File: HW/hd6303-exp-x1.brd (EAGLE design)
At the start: 100 x 80 mm, 40 parts, among them IC1 74HC245N, IC2 74HC245N, IC3 74HC245N, IC4 LM386N-1

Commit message: pullup for page_a13-page_a17, fixed decoder rom
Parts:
- C1, C10, C3, C4, C5, C6, C7, C8, C9: value (none) -> 100n
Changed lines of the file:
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@@
 <attribute name="NAME" x="12.065" y="18.415" size="1.27" layer="26" rot="MR270"/>
 </element>
-<element name="C4" library="rcl" package="C0603" value="" x="66.04" y="5.08" smashed="yes" rot="MR180">
+<element name="C4" library="rcl" package="C0603" value="100n" x="66.04" y="5.08" smashed="yes" rot="MR180">
 <attribute name="NAME" x="65.405" y="4.445" size="1.27" layer="26" rot="MR180"/>
 <attribute name="VALUE" x="65.405" y="6.985" size="1.27" layer="28" rot="MR180"/>
 </element>
-<element name="C5" library="rcl" package="C0603" value="" x="62.23" y="43.18" smashed="yes" rot="MR270">
+<element name="C5" library="rcl" package="C0603" value="100n" x="62.23" y="43.18" smashed="yes" rot="MR270">
 <attribute name="NAME" x="61.595" y="43.815" size="1.27" layer="26" rot="MR270"/>
 <attribute name="VALUE" x="64.135" y="43.815" size="1.27" layer="28" rot="MR270"/>
 </element>
-<element name="C6" library="rcl" package="C0603" value="" x="15.24" y="16.51" smashed="yes" rot="MR90">
+<element name="C6" library="rcl" package="C0603" value="100n" x="15.24" y="16.51" smashed="yes" rot="MR90">
 <attribute name="NAME" x="15.875" y="15.875" size="1.27" layer="26" rot="MR90"/>
 <attribute name="VALUE" x="13.335" y="15.875" size="1.27" layer="28" rot="MR90"/>
 </element>
-<element name="C7" library="rcl" package="C0603" value="" x="24.13" y="17.78" smashed="yes" rot="MR90">
+<element name="C7" library="rcl" package="C0603" value="100n" x="24.13" y="17.78" smashed="yes" rot="MR90">
 <attribute name="NAME" x="24.765" y="17.145" size="1.27" layer="26" rot="MR90"/>
 <attribute name="VALUE" x="22.225" y="17.145" size="1.27" layer="28" rot="MR90"/>
 </element>
-<element name="C8" library="rcl" package="C0603" value="" x="12.7" y="54.61" smashed="yes" rot="MR90">
+<element name="C8" library="rcl" package="C0603" value="100n" x="12.7" y="54.61" smashed="yes" rot="MR90">
 <attribute name="NAME" x="13.335" y="53.975" size="1.27" layer="26" rot="MR90"/>
 <attribute name="VALUE" x="10.795" y="53.975" size="1.27" layer="28" rot="MR90"/>
 </element>
-<element name="C9" library="rcl" package="C0603" value="" x="24.13" y="54.61" smashed="yes" rot="MR90">
+<element name="C9" library="rcl" package="C0603" value="100n" x="24.13" y="54.61" smashed="yes" rot="MR90">
 <attribute name="NAME" x="24.765" y="53.975" size="1.27" layer="26" rot="MR90"/>
 <attribute name="VALUE" x="22.225" y="53.975" size="1.27" layer="28" rot="MR90"/>
 </element>
-<element name="C10" library="rcl" package="C0603" value="" x="81.28" y="46.99" smashed="yes" rot="MR180">
+<element name="C10" library="rcl" package="C0603" value="100n" x="81.28" y="46.99" smashed="yes" rot="MR180">
 <attribute name="NAME" x="80.645" y="46.355" size="1.27" layer="26" rot="MR180"/>
 <attribute name="VALUE" x="80.645" y="48.895" size="1.27" layer="28" rot="MR180"/>
@@
 <attribute name="NAME" x="53.34" y="6.35" size="1.27" layer="26" rot="MR0"/>
 </element>
-<element name="C1" library="rcl" package="C0603" value="" x="81.28" y="5.08" smashed="yes" rot="MR180">
+<element name="C1" library="rcl" package="C0603" value="100n" x="81.28" y="5.08" smashed="yes" rot="MR180">
 <attribute name="NAME" x="80.645" y="4.445" size="1.27" layer="26" rot="MR180"/>
 <attribute name="VALUE" x="80.645" y="6.985" size="1.27" layer="28" rot="MR180"/>
@@
 <attribute name="NAME" x="38.1" y="52.07" size="1.27" layer="26" rot="MR90"/>
 </element>
-<element name="C3" library="rcl" package="C0603" value="" x="53.34" y="62.23" smashed="yes" rot="MR270">
+<element name="C3" library="rcl" package="C0603" value="100n" x="53.34" y="62.23" smashed="yes" rot="MR270">
 <attribute name="NAME" x="52.705" y="62.865" size="1.27" layer="26" rot="MR270"/>
 <attribute name="VALUE" x="55.245" y="62.865" size="1.27" layer="28" rot="MR270"/>

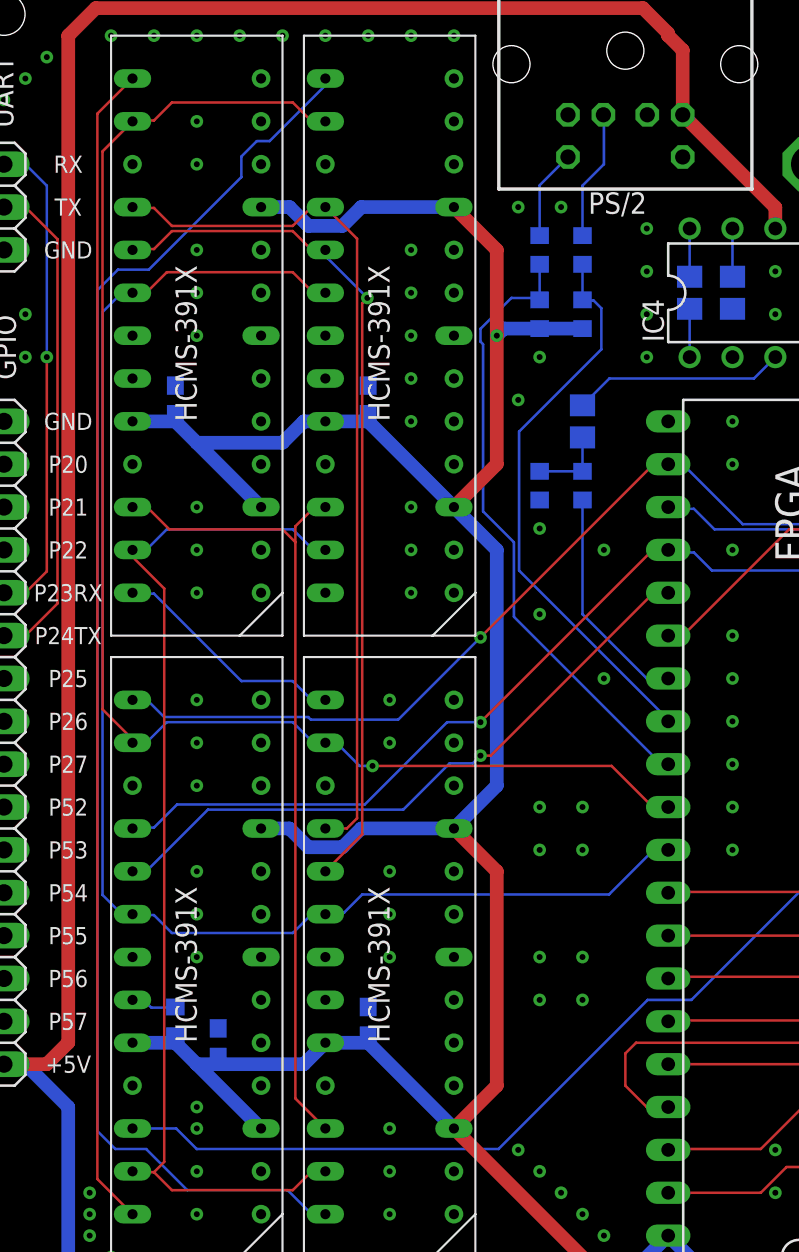
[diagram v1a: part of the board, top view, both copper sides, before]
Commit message: fixed missed nets
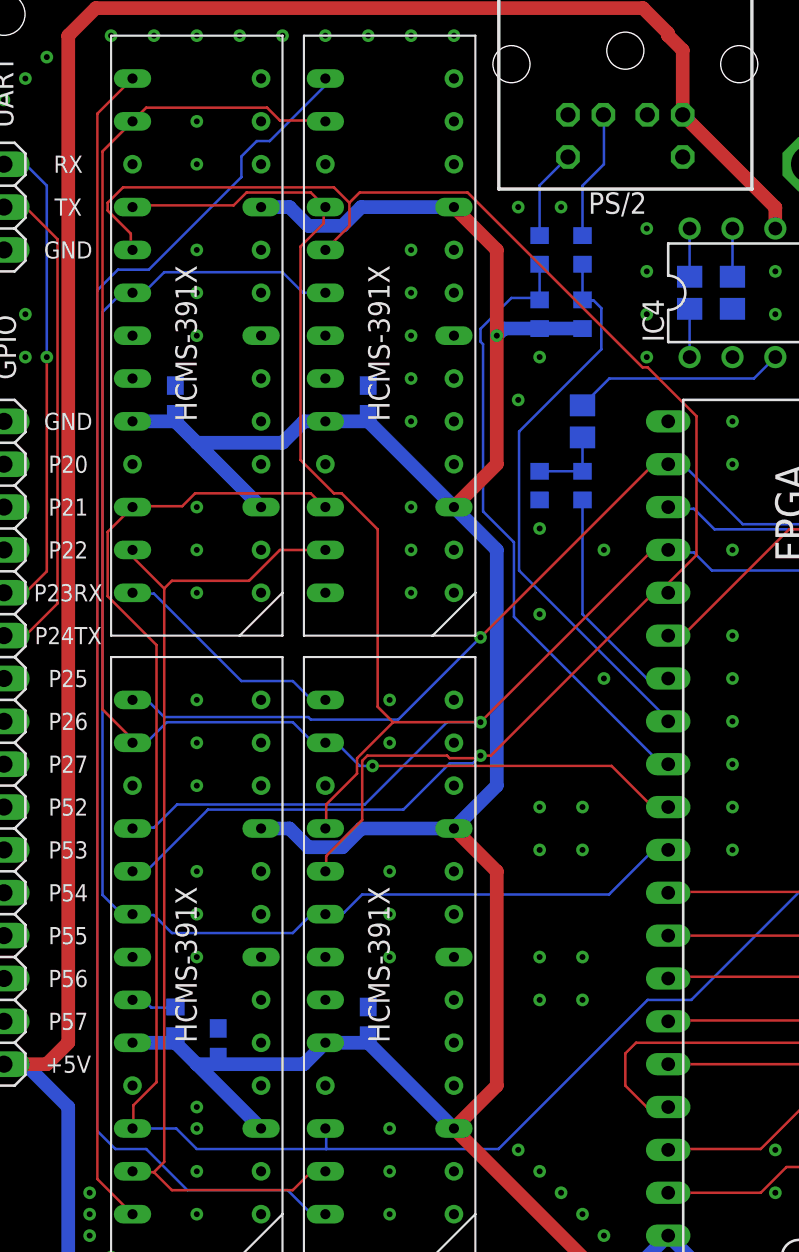
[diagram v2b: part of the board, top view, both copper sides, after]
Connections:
- removed net CE: U$2.18, U$3.18, U$4.18
- removed net CLOCK: U$2.17, U$3.17, U$4.17
- removed net RESET: U$2.24, U$3.24, U$4.24
- net E_RES: now also U$2.24, U$3.24, U$4.24
- net MSCK: now also U$2.17, U$3.17, U$4.17
- net NSS0: now also U$2.18, U$3.18, U$4.18
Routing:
- net NSS0: track 38.6 -> 112.7 mm
- net MSCK: track 76.5 -> 135.5 mm
- net E_RES: track 86.1 -> 138.7 mm
- net CLOCK: track 51.5 -> 0.00 mm
- net CE: track 51.2 -> 0.00 mm, vias 1 -> 0
- net RESET: track 49.2 -> 0.00 mm
- net OSC: track 62.7 -> 60.9 mm

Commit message: released in pcb
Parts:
- added SPI: (no value), pinhead:1X08
- moved UART 55.9 mm to (2.54, 10.2)
- moved SPK 2.84 mm to (59.7, 57.1)
- moved C24 2.29 mm to (57.8, 62.2)
- moved SDMMC 1.91 mm to (78.1, 80.0)
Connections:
- removed net BLANK: STEPFPGA.31, U$1.19, U$2.19, U$3.19, U$4.19
- new net NSS2: SPI.4, STEPFPGA.31
- net +5V: now also SPI.1
- net E_RES: now also SPI.3
- net GND: now also SPI.8, U$1.19, U$2.19, U$3.19, U$4.19
- net MISO: now also SPI.6
- net MOSI: now also SPI.7
- net MSCK: now also SPI.5
- net VCC: now also SPI.2
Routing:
- net BLANK: track 85.9 -> 0.00 mm
- net MISO: track 32.6 -> 112.7 mm
- net NSS2: track 0.00 -> 60.8 mm, vias 0 -> 1
- net MOSI: track 85.5 -> 138.3 mm, vias 1 -> 2
- net MSCK: track 135.5 -> 178.7 mm, vias 1 -> 0
- net RS: track 84.8 -> 119.5 mm, vias 1 -> 0
- net E_RES: track 138.7 -> 158.7 mm, vias 0 -> 3
- net N$3: track 85.0 -> 69.0 mm
- net VCC: track 280.2 -> 290.4 mm
- net NSS0: track 112.7 -> 104.0 mm, vias 1 -> 2
- net P23: track 29.0 -> 36.3 mm, vias 1 -> 2
- net P24: track 29.5 -> 36.6 mm, vias 0 -> 1
- net +5V: track 226.9 -> 231.7 mm
- net N$7: track 10.5 -> 8.11 mm
- net NSS1: track 49.1 -> 47.2 mm
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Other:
- board text added: "+3.3V"
- board text added: "MISO"
- board text added: "MOSI"
- board text added: "MSCK"
- board text added: "NSS2"
- board text added: "RES"

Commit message: fix
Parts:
- added C14, C15, C16, C17: 100n, rcl:C0603
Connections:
- net +5V: now also C14.1, C15.1, C16.1, C17.1, U$1.10, U$1.3, U$2.10, U$2.3, U$3.10, U$3.3, U$4.10, U$4.3
- net GND: now also C14.2, C15.2, C16.2, C17.2
- net VCC: no longer U$1.10, U$1.3, U$2.10, U$2.3, U$3.10, U$3.3, U$4.10, U$4.3
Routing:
- net +5V: track 231.7 -> 353.3 mm, vias 0 -> 1
- net VCC: track 290.4 -> 254.2 mm, vias 1 -> 0
- net RS: track 119.5 -> 84.8 mm
- net E_RES: track 158.7 -> 160.3 mm
- net MSCK: track 178.7 -> 180.0 mm
- net MOSI: track 138.3 -> 139.1 mm
